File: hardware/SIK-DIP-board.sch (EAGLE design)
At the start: 72 parts

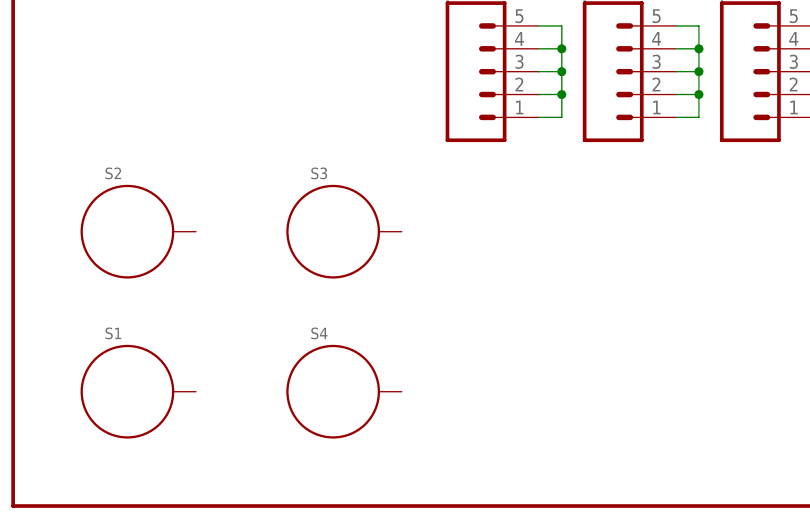
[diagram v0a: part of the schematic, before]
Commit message: Added pads to allow grounding via mounting holes.
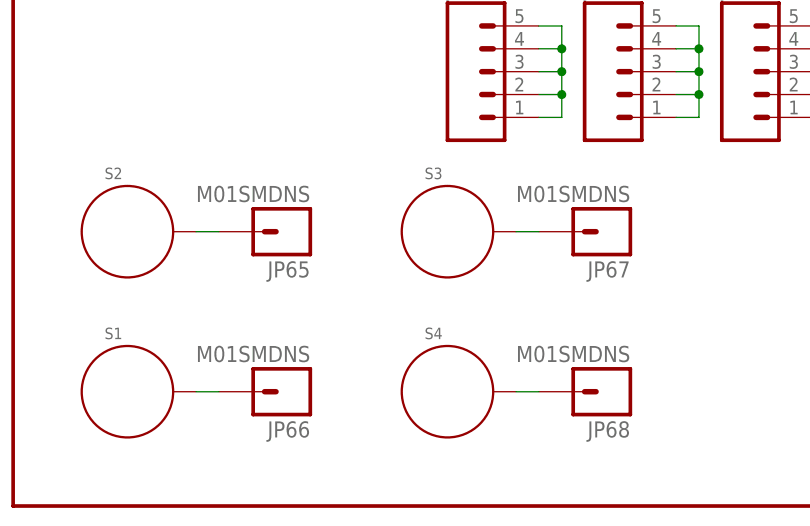
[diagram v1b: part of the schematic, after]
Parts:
- added JP65, JP66, JP67, JP68: M01SMDNS, SparkFun-Connectors:M01SMDNS
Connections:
- new net N$65: JP65.1, S2.P$1
- new net N$66: JP66.1, S1.P$1
- new net N$67: JP67.1, S3.P$1
- new net N$68: JP68.1, S4.P$1
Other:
- moved on the sheet: S3, S4
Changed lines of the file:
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@@
 <part name="JP4" library="SparkFun-Connectors" deviceset="M29" device="NO_SILK"/>
 <part name="LOGO3" library="SparkFun-Aesthetics" deviceset="OSHW-LOGO" device="S"/>
+<part name="JP65" library="SparkFun-Connectors" deviceset="M01" device="SMDNS"/>
+<part name="JP66" library="SparkFun-Connectors" deviceset="M01" device="SMDNS"/>
+<part name="JP67" library="SparkFun-Connectors" deviceset="M01" device="SMDNS"/>
+<part name="JP68" library="SparkFun-Connectors" deviceset="M01" device="SMDNS"/>
 </parts>
 <sheets>
@@
 <instance part="S1" gate="G$1" x="12.7" y="12.7"/>
 <instance part="S2" gate="G$1" x="12.7" y="30.48"/>
-<instance part="S3" gate="G$1" x="35.56" y="30.48"/>
-<instance part="S4" gate="G$1" x="35.56" y="12.7"/>
+<instance part="S3" gate="G$1" x="48.26" y="30.48"/>
+<instance part="S4" gate="G$1" x="48.26" y="12.7"/>
 <instance part="JP10" gate="G$1" x="111.76" y="165.1"/>
 <instance part="JP5" gate="G$1" x="187.96" y="165.1"/>
@@
 <instance part="JP4" gate="G$1" x="228.6" y="132.08"/>
 <instance part="LOGO3" gate="G$1" x="132.08" y="12.7"/>
+<instance part="JP65" gate="G$1" x="30.48" y="30.48" rot="R180"/>
+<instance part="JP66" gate="G$1" x="30.48" y="12.7" rot="R180"/>
+<instance part="JP67" gate="G$1" x="66.04" y="30.48" rot="R180"/>
+<instance part="JP68" gate="G$1" x="66.04" y="12.7" rot="R180"/>
 </instances>
 <busses>
@@
 </segment>
 </net>
+<net name="N$65" class="0">
+<segment>
+<pinref part="S2" gate="G$1" pin="P$1"/>
+<pinref part="JP65" gate="G$1" pin="1"/>
+<wire x1="20.32" y1="30.48" x2="22.86" y2="30.48" width="0.1524" layer="91"/>
+</segment>
+</net>
+<net name="N$66" class="0">
+<segment>
+<pinref part="S1" gate="G$1" pin="P$1"/>
+<pinref part="JP66" gate="G$1" pin="1"/>
+<wire x1="20.32" y1="12.7" x2="22.86" y2="12.7" width="0.1524" layer="91"/>
+</segment>
+</net>
+<net name="N$67" class="0">
+<segment>
+<pinref part="S3" gate="G$1" pin="P$1"/>
+<pinref part="JP67" gate="G$1" pin="1"/>
+<wire x1="55.88" y1="30.48" x2="58.42" y2="30.48" width="0.1524" layer="91"/>
+</segment>
+</net>
+<net name="N$68" class="0">
+<segment>
+<pinref part="S4" gate="G$1" pin="P$1"/>
+<pinref part="JP68" gate="G$1" pin="1"/>
+<wire x1="55.88" y1="12.7" x2="58.42" y2="12.7" width="0.1524" layer="91"/>
+</segment>
+</net>

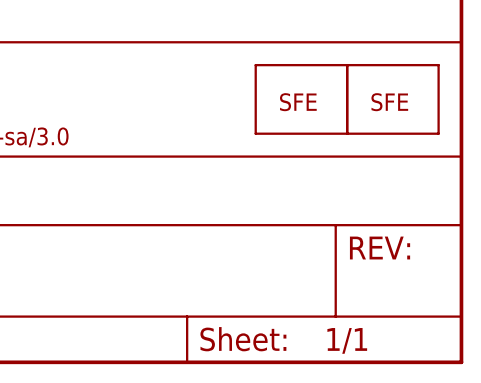
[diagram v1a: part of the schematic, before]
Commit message: Amended following group review
Adjusted size so silk doesn't overlap mounting holes.
Duplicated top silk on bottom.
Added name.
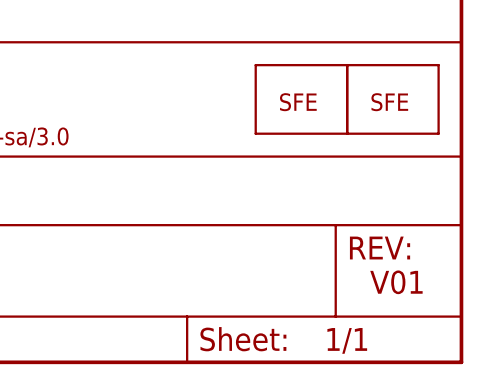
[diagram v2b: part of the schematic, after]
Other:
- note added: "V01"
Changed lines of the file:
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@@
 <plain>
 <text x="167.64" y="10.16" size="2.54" layer="94">Byron Jacquot</text>
+<text x="238.76" y="7.62" size="2.54" layer="94">V01</text>
 </plain>
 <instances>

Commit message: Changed after reviewing prototype
Reversed text on bottom silk layer.
Shrunk overall dimension.
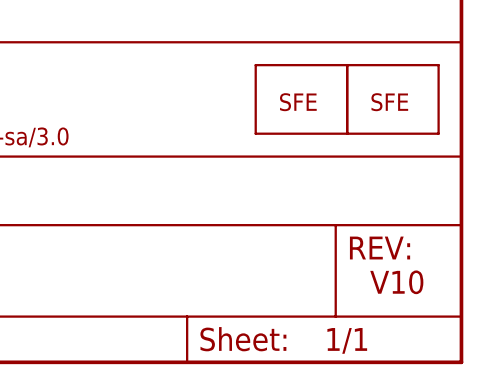
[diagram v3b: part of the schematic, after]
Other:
- note added: "V10"
- note removed: "V01"
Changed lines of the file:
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@@
 <?xml version="1.0" encoding="utf-8"?>
 <!DOCTYPE eagle SYSTEM "eagle.dtd">
-<eagle version="6.0">
+<eagle version="6.5.0">
 <drawing>
 <settings>
@@
 <plain>
 <text x="167.64" y="10.16" size="2.54" layer="94">Byron Jacquot</text>
-<text x="238.76" y="7.62" size="2.54" layer="94">V01</text>
+<text x="238.76" y="7.62" size="2.54" layer="94">V10</text>
 </plain>
 <instances>
